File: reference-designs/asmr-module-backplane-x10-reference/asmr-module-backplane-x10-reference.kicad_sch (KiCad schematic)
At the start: 45 parts, among them J1 PCI-36P, J10 PCI-36P, J2 PCI-36P, J3 PCI-36P, J4 PCI-36P, J5 PCI-36P, J6 PCI-36P, J7 PCI-36P, J8 PCI-36P, J9 PCI-36P

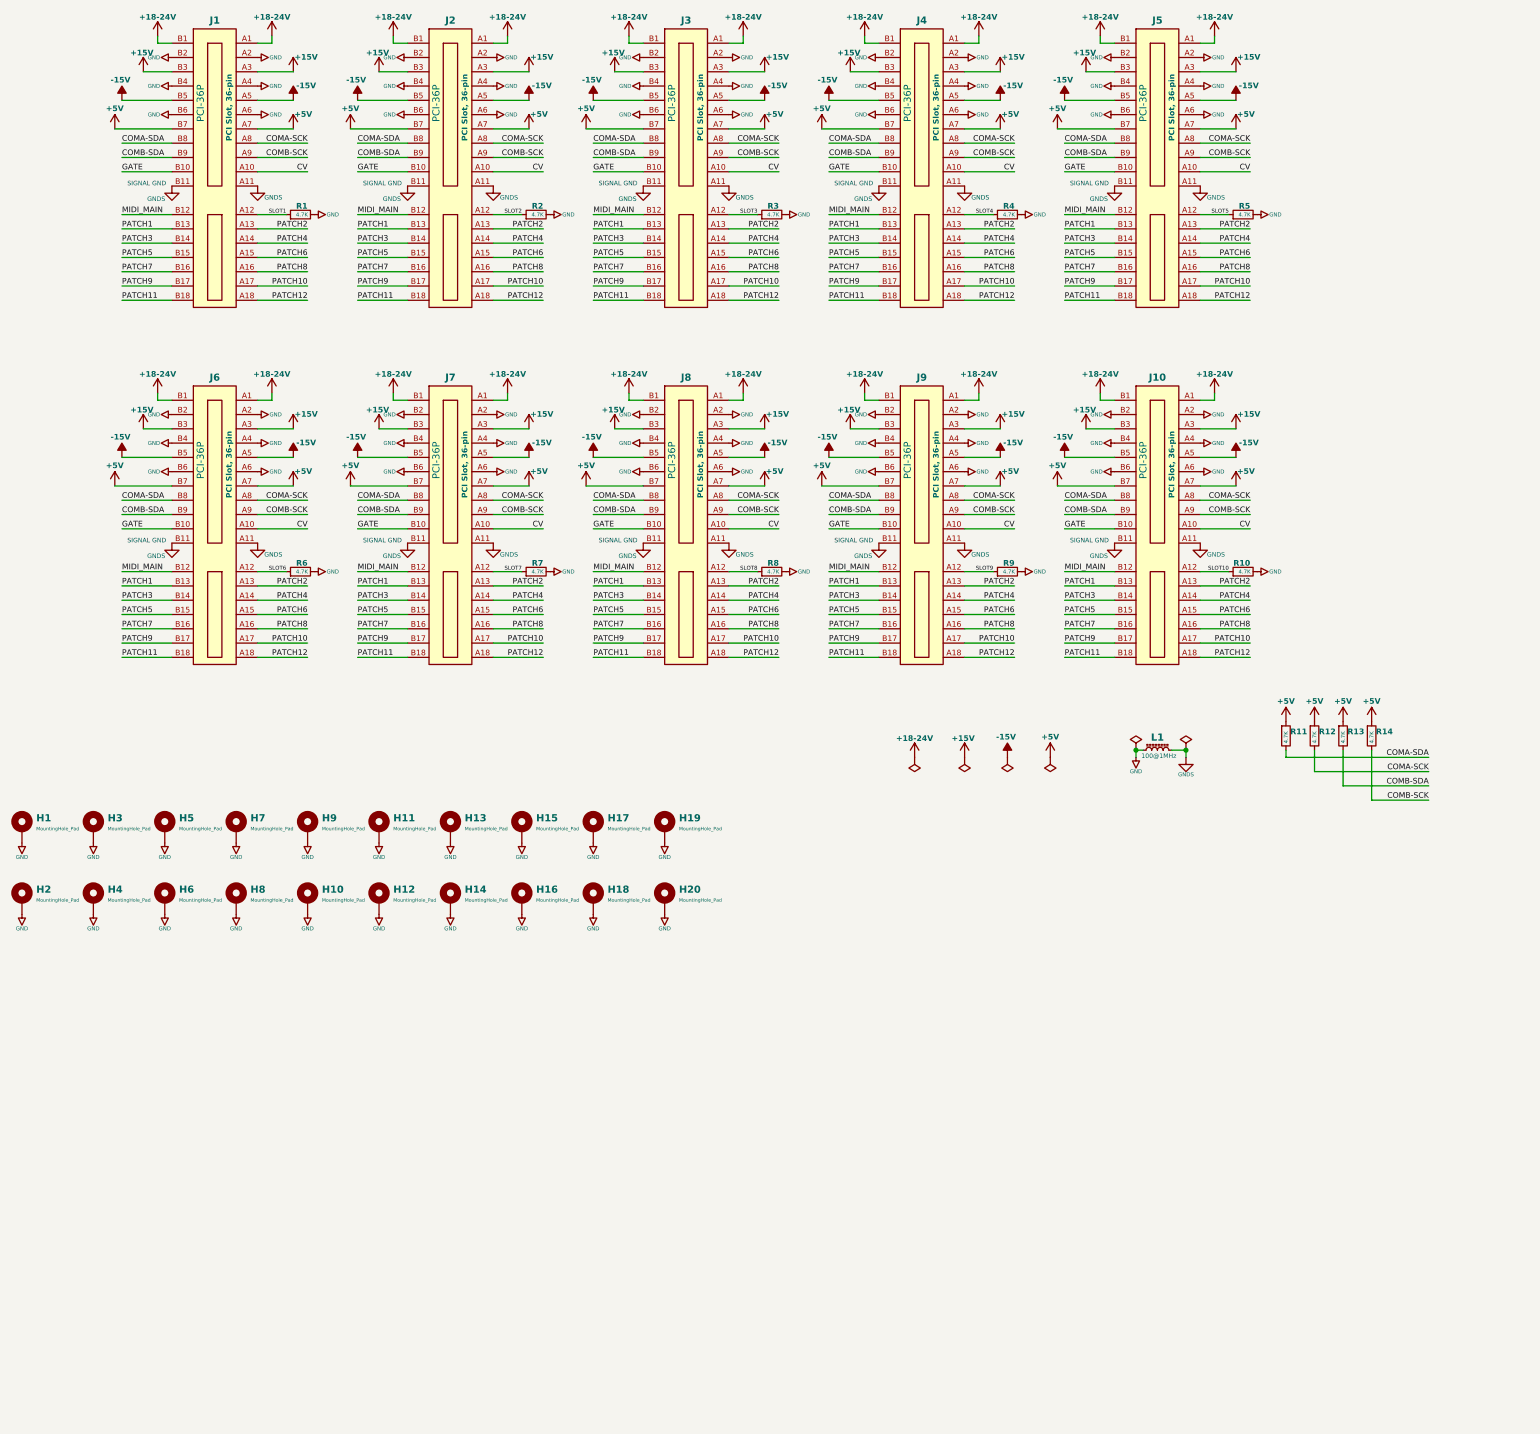
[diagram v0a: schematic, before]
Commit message: Redesign backplane for 64 pin connector.
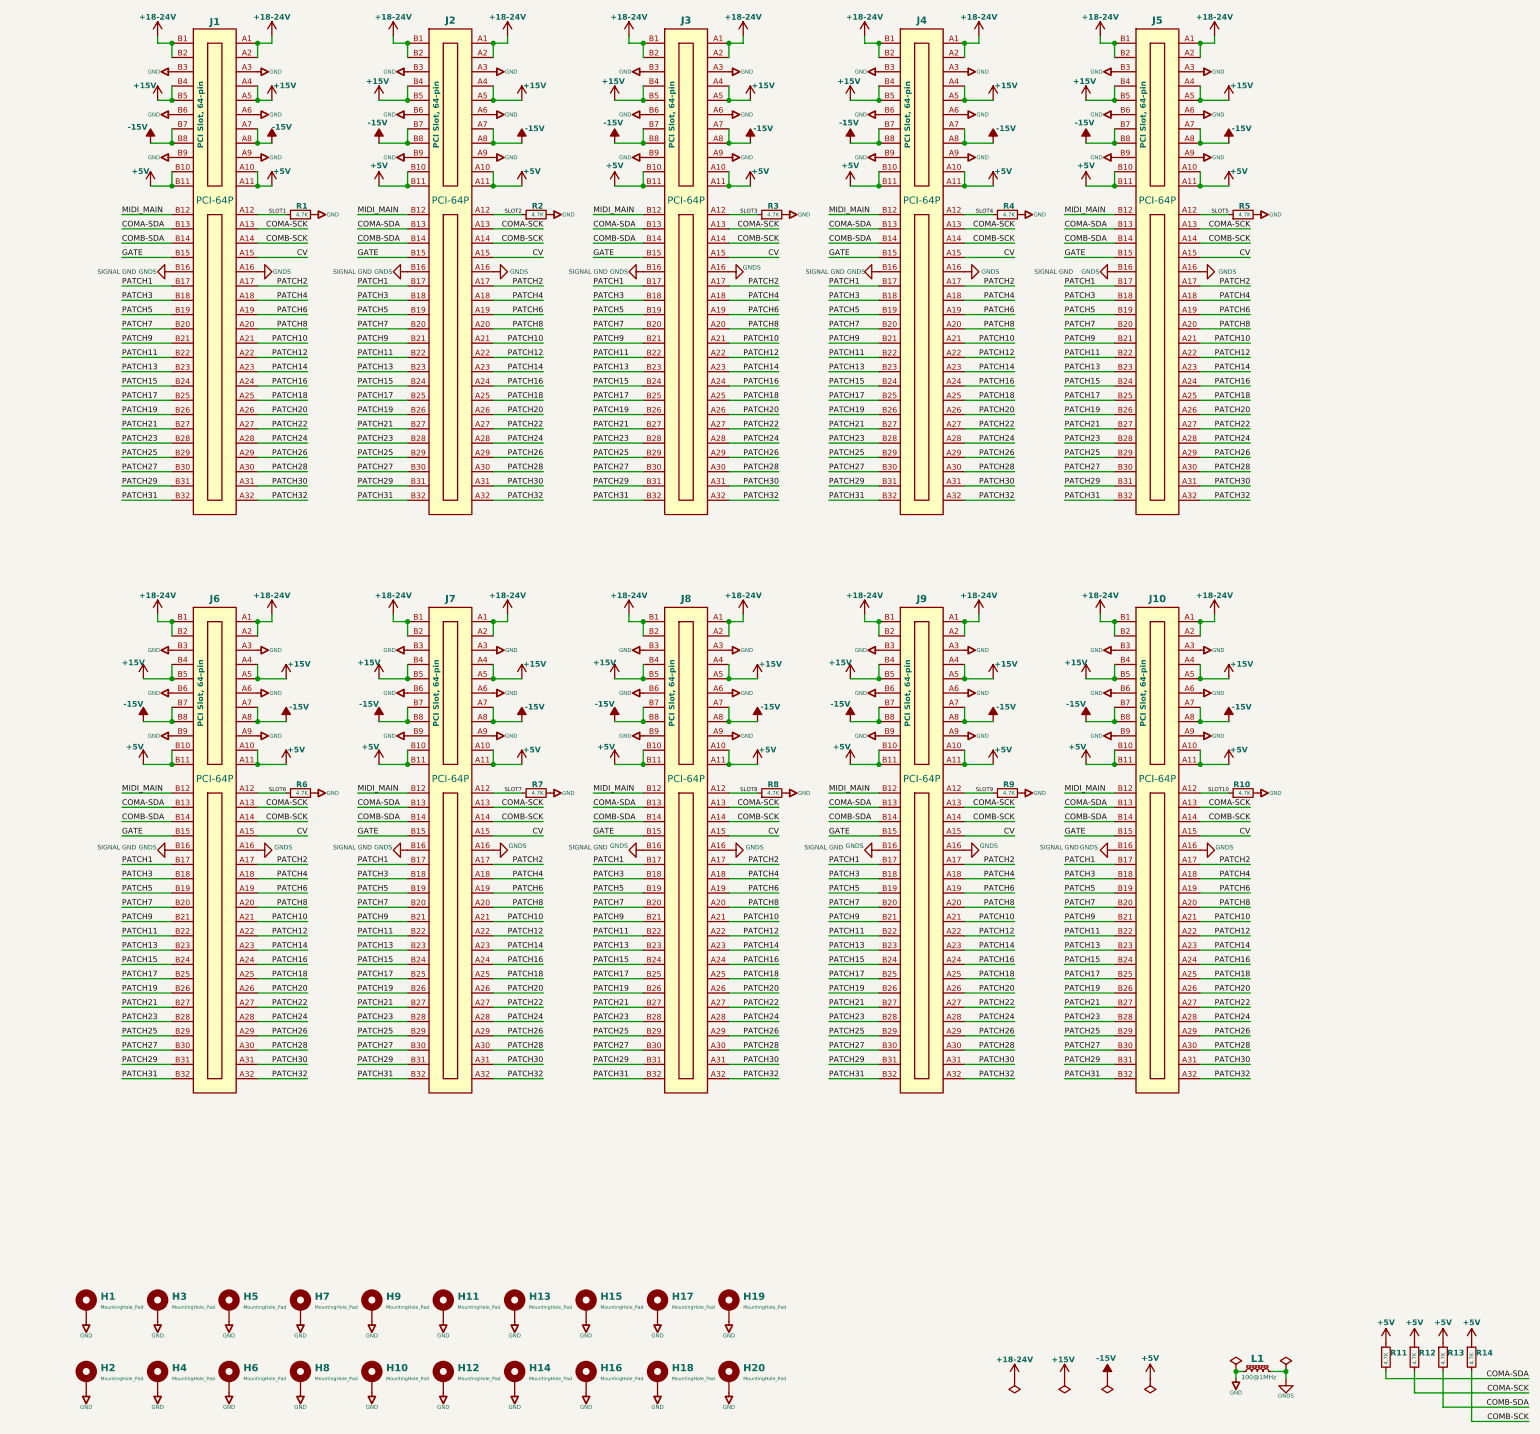
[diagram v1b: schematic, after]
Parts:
- J1, J10, J2, J3, J4, J5, J6, J7, J8, J9: value PCI-36P -> PCI-64P; footprint CM_Connector_Edge:PCI-Slot-36-THD-FCI-10018783 -> CM_Connector_Edge:PCI-Slot-64-THD-FCI-10018784; symbol CM_Connector_Edge:PCIe-36 -> CM_Connector_Edge:PCIe-64; MFR (none) -> Amphenol-FCI; MPN (none) -> 10018783-10201TLF
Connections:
- net +15V: now also J1.A4, J1.A5, J1.B4, J1.B5, J10.A4, J10.A5, J10.B4, J10.B5, J2.A4, J2.A5, J2.B4, J2.B5, J3.A4, J3.A5, J3.B4, J3.B5, J4.A4, J4.A5, J4.B4, J4.B5, J5.A4, J5.A5, J5.B4, J5.B5, J6.A4, J6.A5, J6.B4, J6.B5, J7.A4, J7.A5, J7.B4, J7.B5, J8.A4, J8.A5, J8.B4, J8.B5, J9.A4, J9.A5, J9.B4, J9.B5; no longer J1.A3, J1.B3, J10.A3, J10.B3, J2.A3, J2.B3, J3.A3, J3.B3, J4.A3, J4.B3, J5.A3, J5.B3, J6.A3, J6.B3, J7.A3, J7.B3, J8.A3, J8.B3, J9.A3, J9.B3
- net +18-24V: now also J1.A2, J1.B2, J10.A2, J10.B2, J2.A2, J2.B2, J3.A2, J3.B2, J4.A2, J4.B2, J5.A2, J5.B2, J6.A2, J6.B2, J7.A2, J7.B2, J8.A2, J8.B2, J9.A2, J9.B2
- net +5V: now also J1.A10, J1.A11, J1.B10, J1.B11, J10.A10, J10.A11, J10.B10, J10.B11, J2.A10, J2.A11, J2.B10, J2.B11, J3.A10, J3.A11, J3.B10, J3.B11, J4.A10, J4.A11, J4.B10, J4.B11, J5.A10, J5.A11, J5.B10, J5.B11, J6.A10, J6.A11, J6.B10, J6.B11, J7.A10, J7.A11, J7.B10, J7.B11, J8.A10, J8.A11, J8.B10, J8.B11, J9.A10, J9.A11, J9.B10, J9.B11; no longer J1.A7, J1.B7, J10.A7, J10.B7, J2.A7, J2.B7, J3.A7, J3.B7, J4.A7, J4.B7, J5.A7, J5.B7, J6.A7, J6.B7, J7.A7, J7.B7, J8.A7, J8.B7, J9.A7, J9.B7
- net -15V: now also J1.A7, J1.A8, J1.B7, J1.B8, J10.A7, J10.A8, J10.B7, J10.B8, J2.A7, J2.A8, J2.B7, J2.B8, J3.A7, J3.A8, J3.B7, J3.B8, J4.A7, J4.A8, J4.B7, J4.B8, J5.A7, J5.A8, J5.B7, J5.B8, J6.A7, J6.A8, J6.B7, J6.B8, J7.A7, J7.A8, J7.B7, J7.B8, J8.A7, J8.A8, J8.B7, J8.B8, J9.A7, J9.A8, J9.B7, J9.B8; no longer J1.A5, J1.B5, J10.A5, J10.B5, J2.A5, J2.B5, J3.A5, J3.B5, J4.A5, J4.B5, J5.A5, J5.B5, J6.A5, J6.B5, J7.A5, J7.B5, J8.A5, J8.B5, J9.A5, J9.B5
- net COMA-SCK: now also J1.A13, J10.A13, J2.A13, J3.A13, J4.A13, J5.A13, J6.A13, J7.A13, J8.A13, J9.A13; no longer J1.A8, J10.A8, J2.A8, J3.A8, J4.A8, J5.A8, J6.A8, J7.A8, J8.A8, J9.A8
- net COMA-SDA: now also J1.B13, J10.B13, J2.B13, J3.B13, J4.B13, J5.B13, J6.B13, J7.B13, J8.B13, J9.B13; no longer J1.B8, J10.B8, J2.B8, J3.B8, J4.B8, J5.B8, J6.B8, J7.B8, J8.B8, J9.B8
- net COMB-SCK: now also J1.A14, J10.A14, J2.A14, J3.A14, J4.A14, J5.A14, J6.A14, J7.A14, J8.A14, J9.A14; no longer J1.A9, J10.A9, J2.A9, J3.A9, J4.A9, J5.A9, J6.A9, J7.A9, J8.A9, J9.A9
- net COMB-SDA: now also J1.B14, J10.B14, J2.B14, J3.B14, J4.B14, J5.B14, J6.B14, J7.B14, J8.B14, J9.B14; no longer J1.B9, J10.B9, J2.B9, J3.B9, J4.B9, J5.B9, J6.B9, J7.B9, J8.B9, J9.B9
- net CV: now also J1.A15, J10.A15, J2.A15, J3.A15, J4.A15, J5.A15, J6.A15, J7.A15, J8.A15, J9.A15; no longer J1.A10, J10.A10, J2.A10, J3.A10, J4.A10, J5.A10, J6.A10, J7.A10, J8.A10, J9.A10
- net GATE: now also J1.B15, J10.B15, J2.B15, J3.B15, J4.B15, J5.B15, J6.B15, J7.B15, J8.B15, J9.B15; no longer J1.B10, J10.B10, J2.B10, J3.B10, J4.B10, J5.B10, J6.B10, J7.B10, J8.B10, J9.B10
- net GND: now also J1.A3, J1.A9, J1.B3, J1.B9, J10.A3, J10.A9, J10.B3, J10.B9, J2.A3, J2.A9, J2.B3, J2.B9, J3.A3, J3.A9, J3.B3, J3.B9, J4.A3, J4.A9, J4.B3, J4.B9, J5.A3, J5.A9, J5.B3, J5.B9, J6.A3, J6.A9, J6.B3, J6.B9, J7.A3, J7.A9, J7.B3, J7.B9, J8.A3, J8.A9, J8.B3, J8.B9, J9.A3, J9.A9, J9.B3, J9.B9; no longer J1.A2, J1.A4, J1.B2, J1.B4, J10.A2, J10.A4, J10.B2, J10.B4, J2.A2, J2.A4, J2.B2, J2.B4, J3.A2, J3.A4, J3.B2, J3.B4, J4.A2, J4.A4, J4.B2, J4.B4, J5.A2, J5.A4, J5.B2, J5.B4, J6.A2, J6.A4, J6.B2, J6.B4, J7.A2, J7.A4, J7.B2, J7.B4, J8.A2, J8.A4, J8.B2, J8.B4, J9.A2, J9.A4, J9.B2, J9.B4
- net GNDS: now also J1.A16, J1.B16, J10.A16, J10.B16, J2.A16, J2.B16, J3.A16, J3.B16, J4.A16, J4.B16, J5.A16, J5.B16, J6.A16, J6.B16, J7.A16, J7.B16, J8.A16, J8.B16, J9.A16, J9.B16; no longer J1.A11, J1.B11, J10.A11, J10.B11, J2.A11, J2.B11, J3.A11, J3.B11, J4.A11, J4.B11, J5.A11, J5.B11, J6.A11, J6.B11, J7.A11, J7.B11, J8.A11, J8.B11, J9.A11, J9.B11
- net PATCH1: now also J1.B17, J10.B17, J2.B17, J3.B17, J4.B17, J5.B17, J6.B17, J7.B17, J8.B17, J9.B17; no longer J1.B13, J10.B13, J2.B13, J3.B13, J4.B13, J5.B13, J6.B13, J7.B13, J8.B13, J9.B13
- net PATCH10: now also J1.A21, J10.A21, J2.A21, J3.A21, J4.A21, J5.A21, J6.A21, J7.A21, J8.A21, J9.A21; no longer J1.A17, J10.A17, J2.A17, J3.A17, J4.A17, J5.A17, J6.A17, J7.A17, J8.A17, J9.A17
- net PATCH11: now also J1.B22, J10.B22, J2.B22, J3.B22, J4.B22, J5.B22, J6.B22, J7.B22, J8.B22, J9.B22; no longer J1.B18, J10.B18, J2.B18, J3.B18, J4.B18, J5.B18, J6.B18, J7.B18, J8.B18, J9.B18
- net PATCH12: now also J1.A22, J10.A22, J2.A22, J3.A22, J4.A22, J5.A22, J6.A22, J7.A22, J8.A22, J9.A22; no longer J1.A18, J10.A18, J2.A18, J3.A18, J4.A18, J5.A18, J6.A18, J7.A18, J8.A18, J9.A18
- net PATCH2: now also J1.A17, J10.A17, J2.A17, J3.A17, J4.A17, J5.A17, J6.A17, J7.A17, J8.A17, J9.A17; no longer J1.A13, J10.A13, J2.A13, J3.A13, J4.A13, J5.A13, J6.A13, J7.A13, J8.A13, J9.A13
- net PATCH3: now also J1.B18, J10.B18, J2.B18, J3.B18, J4.B18, J5.B18, J6.B18, J7.B18, J8.B18, J9.B18; no longer J1.B14, J10.B14, J2.B14, J3.B14, J4.B14, J5.B14, J6.B14, J7.B14, J8.B14, J9.B14
- net PATCH4: now also J1.A18, J10.A18, J2.A18, J3.A18, J4.A18, J5.A18, J6.A18, J7.A18, J8.A18, J9.A18; no longer J1.A14, J10.A14, J2.A14, J3.A14, J4.A14, J5.A14, J6.A14, J7.A14, J8.A14, J9.A14
- net PATCH5: now also J1.B19, J10.B19, J2.B19, J3.B19, J4.B19, J5.B19, J6.B19, J7.B19, J8.B19, J9.B19; no longer J1.B15, J10.B15, J2.B15, J3.B15, J4.B15, J5.B15, J6.B15, J7.B15, J8.B15, J9.B15
- net PATCH6: now also J1.A19, J10.A19, J2.A19, J3.A19, J4.A19, J5.A19, J6.A19, J7.A19, J8.A19, J9.A19; no longer J1.A15, J10.A15, J2.A15, J3.A15, J4.A15, J5.A15, J6.A15, J7.A15, J8.A15, J9.A15
- net PATCH7: now also J1.B20, J10.B20, J2.B20, J3.B20, J4.B20, J5.B20, J6.B20, J7.B20, J8.B20, J9.B20; no longer J1.B16, J10.B16, J2.B16, J3.B16, J4.B16, J5.B16, J6.B16, J7.B16, J8.B16, J9.B16
- net PATCH8: now also J1.A20, J10.A20, J2.A20, J3.A20, J4.A20, J5.A20, J6.A20, J7.A20, J8.A20, J9.A20; no longer J1.A16, J10.A16, J2.A16, J3.A16, J4.A16, J5.A16, J6.A16, J7.A16, J8.A16, J9.A16
- net PATCH9: now also J1.B21, J10.B21, J2.B21, J3.B21, J4.B21, J5.B21, J6.B21, J7.B21, J8.B21, J9.B21; no longer J1.B17, J10.B17, J2.B17, J3.B17, J4.B17, J5.B17, J6.B17, J7.B17, J8.B17, J9.B17
- new net PATCH13: J1.B23, J10.B23, J2.B23, J3.B23, J4.B23, J5.B23, J6.B23, J7.B23, J8.B23, J9.B23
- new net PATCH14: J1.A23, J10.A23, J2.A23, J3.A23, J4.A23, J5.A23, J6.A23, J7.A23, J8.A23, J9.A23
- new net PATCH15: J1.B24, J10.B24, J2.B24, J3.B24, J4.B24, J5.B24, J6.B24, J7.B24, J8.B24, J9.B24
- new net PATCH16: J1.A24, J10.A24, J2.A24, J3.A24, J4.A24, J5.A24, J6.A24, J7.A24, J8.A24, J9.A24
- new net PATCH17: J1.B25, J10.B25, J2.B25, J3.B25, J4.B25, J5.B25, J6.B25, J7.B25, J8.B25, J9.B25
- new net PATCH18: J1.A25, J10.A25, J2.A25, J3.A25, J4.A25, J5.A25, J6.A25, J7.A25, J8.A25, J9.A25
- new net PATCH19: J1.B26, J10.B26, J2.B26, J3.B26, J4.B26, J5.B26, J6.B26, J7.B26, J8.B26, J9.B26
- new net PATCH20: J1.A26, J10.A26, J2.A26, J3.A26, J4.A26, J5.A26, J6.A26, J7.A26, J8.A26, J9.A26
- new net PATCH21: J1.B27, J10.B27, J2.B27, J3.B27, J4.B27, J5.B27, J6.B27, J7.B27, J8.B27, J9.B27
- new net PATCH22: J1.A27, J10.A27, J2.A27, J3.A27, J4.A27, J5.A27, J6.A27, J7.A27, J8.A27, J9.A27
- new net PATCH23: J1.B28, J10.B28, J2.B28, J3.B28, J4.B28, J5.B28, J6.B28, J7.B28, J8.B28, J9.B28
- new net PATCH24: J1.A28, J10.A28, J2.A28, J3.A28, J4.A28, J5.A28, J6.A28, J7.A28, J8.A28, J9.A28
- new net PATCH25: J1.B29, J10.B29, J2.B29, J3.B29, J4.B29, J5.B29, J6.B29, J7.B29, J8.B29, J9.B29
- new net PATCH26: J1.A29, J10.A29, J2.A29, J3.A29, J4.A29, J5.A29, J6.A29, J7.A29, J8.A29, J9.A29
- new net PATCH27: J1.B30, J10.B30, J2.B30, J3.B30, J4.B30, J5.B30, J6.B30, J7.B30, J8.B30, J9.B30
- new net PATCH28: J1.A30, J10.A30, J2.A30, J3.A30, J4.A30, J5.A30, J6.A30, J7.A30, J8.A30, J9.A30
- new net PATCH29: J1.B31, J10.B31, J2.B31, J3.B31, J4.B31, J5.B31, J6.B31, J7.B31, J8.B31, J9.B31
- new net PATCH30: J1.A31, J10.A31, J2.A31, J3.A31, J4.A31, J5.A31, J6.A31, J7.A31, J8.A31, J9.A31
- new net PATCH31: J1.B32, J10.B32, J2.B32, J3.B32, J4.B32, J5.B32, J6.B32, J7.B32, J8.B32, J9.B32
- new net PATCH32: J1.A32, J10.A32, J2.A32, J3.A32, J4.A32, J5.A32, J6.A32, J7.A32, J8.A32, J9.A32
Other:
- moved on the sheet: H1, H10, H11, H12, H13, H14, H15, H16, H17, H18, H19, H2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

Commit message: Update to proper slot detect resistor values.
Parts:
- R1: value 4.7K -> 3.3K
- R10: value 4.7K -> 33.0K
- R2: value 4.7K -> 6.6K
- R3: value 4.7K -> 10K
- R4: value 4.7K -> 13.3K
- R5: value 4.7K -> 16.5K
- R6: value 4.7K -> 20.0K
- R7: value 4.7K -> 23.2K
- R8: value 4.7K -> 26.7K
- R9: value 4.7K -> 30.0K
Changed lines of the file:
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@@
 			)
 		)
-		(property "Value" "4.7K"
+		(property "Value" "30.0K"
 			(at 200.914 160.02 90)
 			(effects
@@
 			)
 		)
-		(property "Value" "4.7K"
+		(property "Value" "3.3K"
 			(at 75.184 57.15 90)
 			(effects
@@
 			)
 		)
-		(property "Value" "4.7K"
+		(property "Value" "26.7K"
 			(at 159.004 160.02 90)
 			(effects
@@
 			)
 		)
-		(property "Value" "4.7K"
+		(property "Value" "33.0K"
 			(at 242.824 160.02 90)
 			(effects
@@
 			)
 		)
-		(property "Value" "4.7K"
+		(property "Value" "6.6K"
 			(at 117.094 57.15 90)
 			(effects
@@
 			)
 		)
-		(property "Value" "4.7K"
+		(property "Value" "23.2K"
 			(at 117.094 160.02 90)
 			(effects
@@
 			)
 		)
-		(property "Value" "4.7K"
+		(property "Value" "16.5K"
 			(at 242.824 57.15 90)
 			(effects
@@
 			)
 		)
-		(property "Value" "4.7K"
+		(property "Value" "10K"
 			(at 159.004 57.15 90)
 			(effects
@@
 			)
 		)
-		(property "Value" "4.7K"
+		(property "Value" "13.3K"
 			(at 200.914 57.15 90)
 			(effects
@@
 			)
 		)
-		(property "Value" "4.7K"
+		(property "Value" "20.0K"
 			(at 75.184 160.02 90)
 			(effects
